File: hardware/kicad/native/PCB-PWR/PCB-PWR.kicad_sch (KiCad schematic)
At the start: 60 parts, among them J1 PWR_INPUT_43045-0213, J2 MAIN_PWR_43045-1202_12PIN, Q1 CSD18540Q5B, U1 LM74700QDBVRQ1, U2 INA226AIDGSR, U3 LMR604403SRAKR 3V8, U4 LMR604403SRAKR 3V3 AON, U5 TPS7A2018PDBVR 1V8_MIC

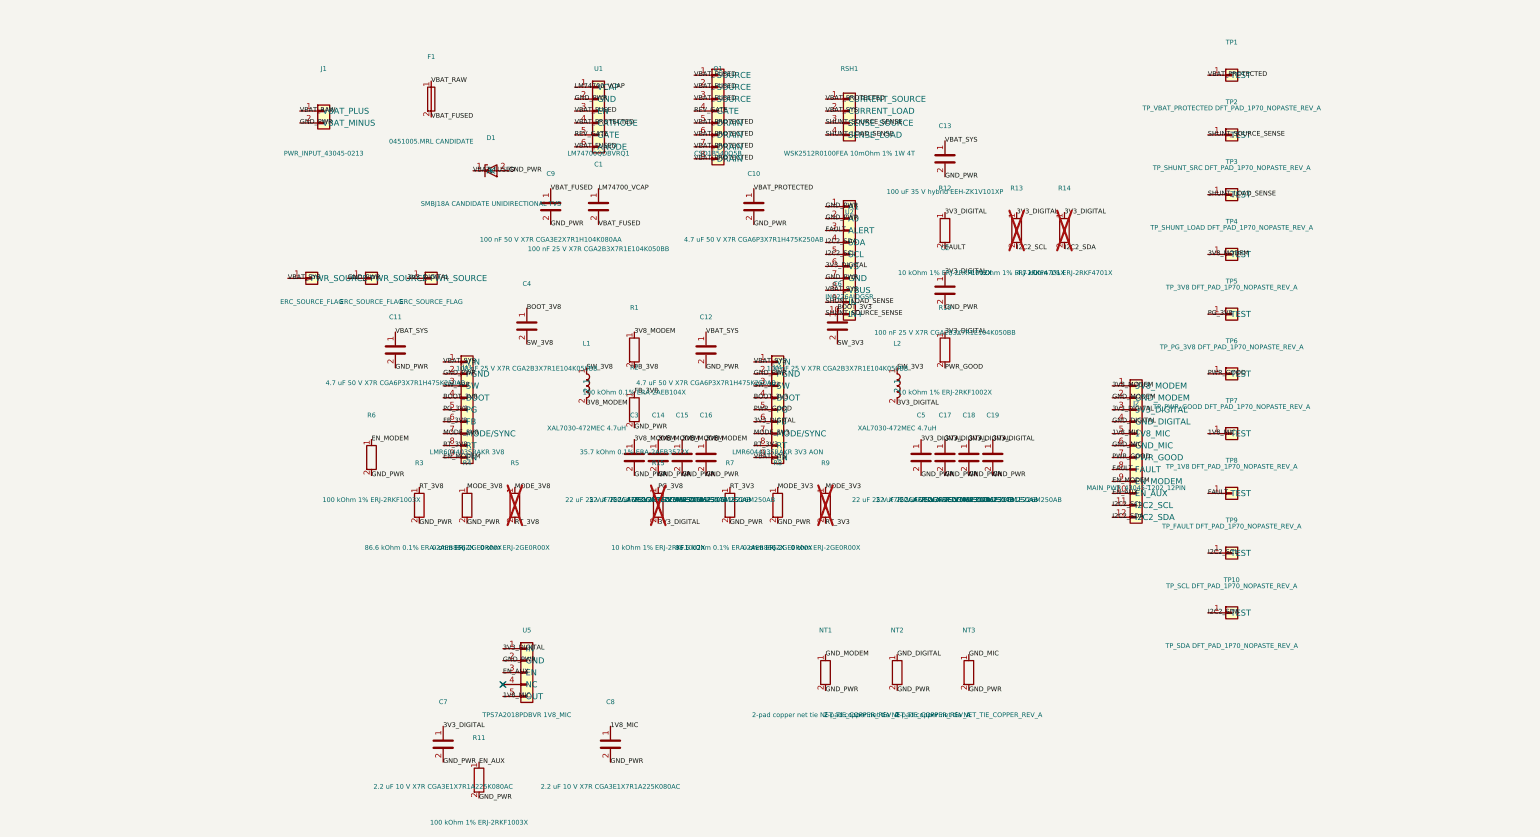
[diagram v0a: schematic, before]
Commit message: hardware: make PCB-PWR schematic reviewable
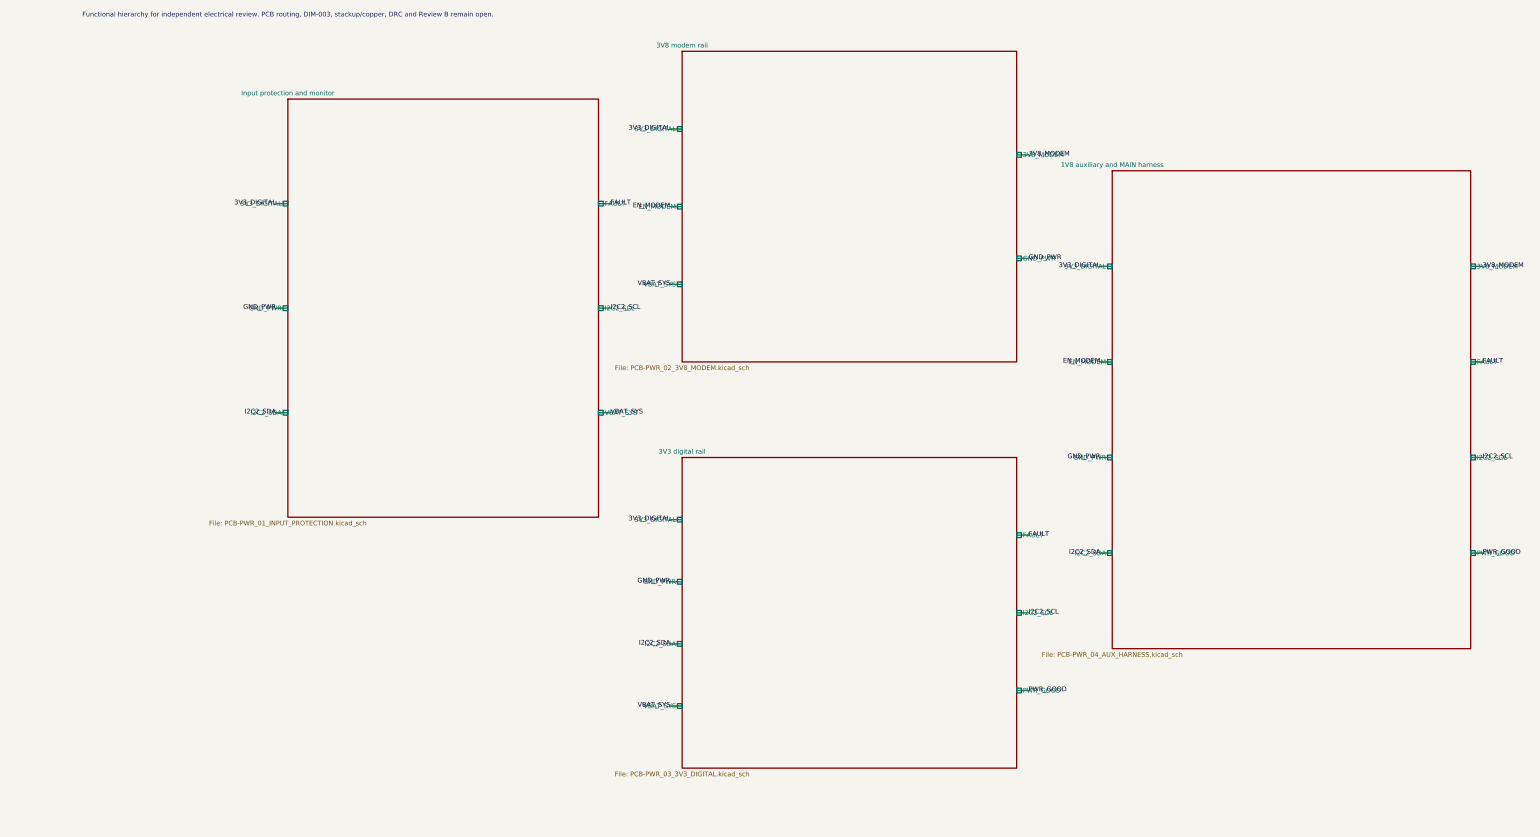
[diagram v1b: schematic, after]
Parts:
- removed C1, C2, C4, C6: 100 nF 25 V X7R CGA2B3X7R1E104K050BB, Capacitor_SMD:C_0402_1005Metric, symbol Device:C
- removed C10, C11, C12: 4.7 uF 50 V X7R CGA6P3X7R1H475K250AB, Capacitor_SMD:C_1210_3225Metric, symbol Device:C
- removed C13: 100 uF 35 V hybrid EEH-ZK1V101XP, Capacitor_SMD:CP_Elec_6.3x7.7, symbol Device:C
- removed C14, C15, C16, C17, C18, C19, C3, C5: 22 uF 25 V X7R CGA6P3X7R1E226M250AB, Capacitor_SMD:C_1210_3225Metric, symbol Device:C
- removed C7, C8: 2.2 uF 10 V X7R CGA3E1X7R1A225K080AC, Capacitor_SMD:C_0603_1608Metric, symbol Device:C
- removed C9: 100 nF 50 V X7R CGA3E2X7R1H104K080AA, Capacitor_SMD:C_0603_1608Metric, symbol Device:C
- removed D1: SMBJ18A CANDIDATE UNIDIRECTIONAL TVS, Diode_SMD:D_SMB, symbol Device:D_Zener
- removed F1: 0451005.MRL CANDIDATE, Fuse:Fuse_1206_3216Metric, symbol Device:Fuse
- removed J1: PWR_INPUT_43045-0213, DioneyaPWR:Molex_43045-0213_MicroFit-2_Vertical, symbol DioneyaPWR:Conn_01x02
- removed J2: MAIN_PWR_43045-1202_12PIN, DioneyaMain:Molex_43045-1202_MicroFit-12_RA, symbol DioneyaPWR:Conn_01x12
- removed L1, L2: XAL7030-472MEC 4.7uH, DioneyaPWR:Coilcraft_XAL7030_472, symbol Device:L
- removed NT1, NT2, NT3: 2-pad copper net tie NET_TIE_COPPER_REV_A, NetTie:NetTie-2_SMD_Pad0.5mm, symbol Device:R
- removed Q1: CSD18540Q5B, DioneyaPWR:CSD18540Q5B_DNK, symbol DioneyaPWR:Conn_01x08
- removed R1: 100 kOhm 0.1% ERA-2AEB104X, Resistor_SMD:R_0402_1005Metric, symbol Device:R
- removed R10, R12, R15: 10 kOhm 1% ERJ-2RKF1002X, Resistor_SMD:R_0402_1005Metric, symbol Device:R
- removed R11, R6: 100 kOhm 1% ERJ-2RKF1003X, Resistor_SMD:R_0402_1005Metric, symbol Device:R
- removed R13, R14: 4.7 kOhm 1% ERJ-2RKF4701X, Resistor_SMD:R_0402_1005Metric, symbol Device:R
- removed R2: 35.7 kOhm 0.1% ERA-2AEB3572X, Resistor_SMD:R_0402_1005Metric, symbol Device:R
- removed R3, R7: 86.6 kOhm 0.1% ERA-2AEB8662X, Resistor_SMD:R_0402_1005Metric, symbol Device:R
- removed R4, R5, R8, R9: 0 ohm ERJ-2GE0R00X, Resistor_SMD:R_0402_1005Metric, symbol Device:R
- removed RSH1: WSK2512R0100FEA 10mOhm 1% 1W 4T, DioneyaPWR:Vishay_WSK2512_4T_T1.19mm, symbol DioneyaPWR:Conn_01x04
- removed TP1: TP_VBAT_PROTECTED DFT_PAD_1P70_NOPASTE_REV_A, DioneyaPWR:TestPoint_DFT_1.7mm_NoPaste, symbol DioneyaPWR:TESTPOINT
- removed TP10: TP_SDA DFT_PAD_1P70_NOPASTE_REV_A, DioneyaPWR:TestPoint_DFT_1.7mm_NoPaste, symbol DioneyaPWR:TESTPOINT
- removed TP2: TP_SHUNT_SRC DFT_PAD_1P70_NOPASTE_REV_A, DioneyaPWR:TestPoint_DFT_1.7mm_NoPaste, symbol DioneyaPWR:TESTPOINT
- removed TP3: TP_SHUNT_LOAD DFT_PAD_1P70_NOPASTE_REV_A, DioneyaPWR:TestPoint_DFT_1.7mm_NoPaste, symbol DioneyaPWR:TESTPOINT
- removed TP4: TP_3V8 DFT_PAD_1P70_NOPASTE_REV_A, DioneyaPWR:TestPoint_DFT_1.7mm_NoPaste, symbol DioneyaPWR:TESTPOINT
- removed TP5: TP_PG_3V8 DFT_PAD_1P70_NOPASTE_REV_A, DioneyaPWR:TestPoint_DFT_1.7mm_NoPaste, symbol DioneyaPWR:TESTPOINT
- removed TP6: TP_PWR_GOOD DFT_PAD_1P70_NOPASTE_REV_A, DioneyaPWR:TestPoint_DFT_1.7mm_NoPaste, symbol DioneyaPWR:TESTPOINT
- removed TP7: TP_1V8 DFT_PAD_1P70_NOPASTE_REV_A, DioneyaPWR:TestPoint_DFT_1.7mm_NoPaste, symbol DioneyaPWR:TESTPOINT
- removed TP8: TP_FAULT DFT_PAD_1P70_NOPASTE_REV_A, DioneyaPWR:TestPoint_DFT_1.7mm_NoPaste, symbol DioneyaPWR:TESTPOINT
- removed TP9: TP_SCL DFT_PAD_1P70_NOPASTE_REV_A, DioneyaPWR:TestPoint_DFT_1.7mm_NoPaste, symbol DioneyaPWR:TESTPOINT
- removed U1: LM74700QDBVRQ1, DioneyaPWR:TI_DBV0006A_SOT23-6, symbol DioneyaPWR:Conn_01x06
- removed U2: INA226AIDGSR, DioneyaPWR:TI_DGS0010A_VSSOP10, symbol DioneyaPWR:Conn_01x10
- removed U3: LMR604403SRAKR 3V8, DioneyaPWR:LMR60440_RAK0009A, symbol DioneyaPWR:Conn_01x09
- removed U4: LMR604403SRAKR 3V3 AON, DioneyaPWR:LMR60440_RAK0009A, symbol DioneyaPWR:Conn_01x09
- removed U5: TPS7A2018PDBVR 1V8_MIC, DioneyaMain:TI_DBV0005A_SOT23-5, symbol DioneyaPWR:Conn_01x05
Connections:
- no-connect marks 1 -> 0
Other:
- added sheet 1V8 auxiliary and MAIN harness (PCB-PWR_04_AUX_HARNESS.kicad_sch)
- added sheet 3V3 digital rail (PCB-PWR_03_3V3_DIGITAL.kicad_sch)
- added sheet 3V8 modem rail (PCB-PWR_02_3V8_MODEM.kicad_sch)
- added sheet Input protection and monitor (PCB-PWR_01_INPUT_PROTECTION.kicad_sch)
- note added: "Functional hierarchy for independent electrical review. PCB routing, DIM-003, stackup/copper, DRC and Review B remain open."
- title: Dioneya EVT-PRE-20 PCB-PWR Rev.A -> Dioneya EVT-PRE-20 PCB-PWR Rev.A - System overview
